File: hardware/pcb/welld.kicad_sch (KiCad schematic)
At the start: 0 parts

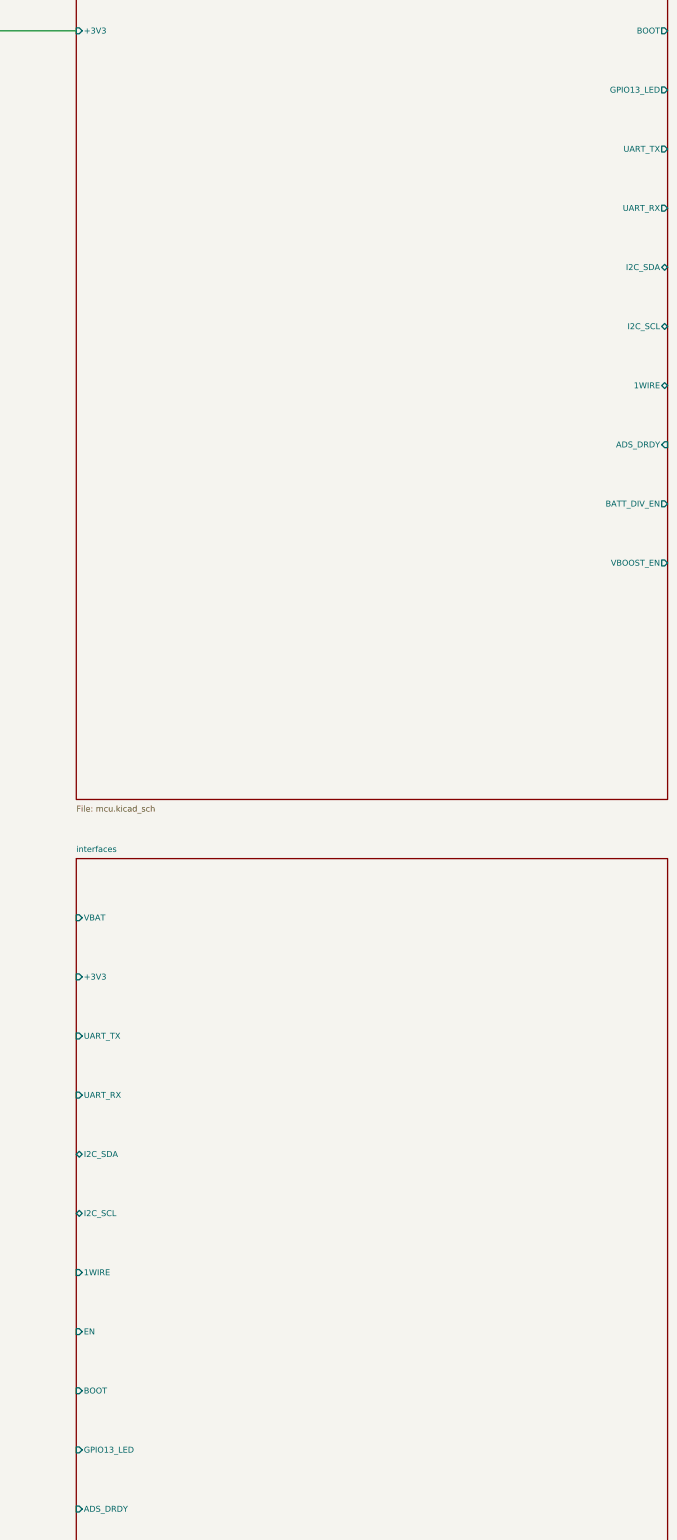
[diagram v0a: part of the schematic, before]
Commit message: hw(pcb): electrical review pass — fix 3V3 regulator variant, boost topology, GPIO13 LED conflict
Full electrical-correctness-gate review of the fresh-start design. Two of
the four CRITICALs from the 2026-05-25 senior review were resolved
incorrectly; this pass corrects them and fixes new findings:

- U1: AP63205WU is the 5 V fixed variant and the R_FBH/R_FBL values
  (560k/124k) assume a 0.6 V reference no AP6320x has — every
  combination overdrives the 3V3 rail. Swap to AP63203WU (3.3 V fixed),
  FB tied to +3V3, R_FBH/R_FBL marked DNP.
- MT3608B VLOOP: documented wiring was a buck topology and the BOM had
  no output rectifier (async boost cannot work without one). Corrected
  to VBAT→L1→SW, added D15 (SS34) and a Q3/Q4 load-disconnect so VBAT
  doesn't leak to the loop terminals through L1+D15 during deep sleep.
- Status LED moved GPIO13 → GPIO14: a green LED + 1k on GPIO13 holds
  the factory-reset strap LOW at boot → NVS wipe every boot. TP13 pad
  added for field factory reset.
- Battery divider reworked to high-side P-FET (Q5): the low-side switch
  left AIN2 biased above ADS1115 VDD through R7 (~14 uA sleep leak).
  C8 100nF → 1nF to fit the firmware's 1 ms enable window.
- TVS D8/D14 SMAJ28CA → SMAJ24CA (zero margin to CN3722 28 V abs max);
  C17 → 35 V/1206; C21 → 50 V; D6 footprint SOD-123 → SMB.
- /CHRG_SOLAR pull-up (R25), VBOOST_EN pull-down (R27), ESP32 EN RC
  (R15/C36) added; C25 duplicate bootstrap cap deleted; C16 assigned as
  U1 VIN bulk.
- schematic_connections.md rewritten pin-name-based with a symbol
  pin-number verification table and datasheet-verification blocker list;
  BOM/placement/guide/placement-script reconciled (phantom refdes,
  wrong ADS1115 pin numbers, mis-documented MPPT divider, shunt return
  path contradiction).

Flagged, not fixed: TP5100 cannot charge 2S from 5 V USB (step-down
charger) — needs an IC swap; schematic still has zero drawn wires; five
IC symbol pinouts pending datasheet verification before ordering.

Co-Auth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
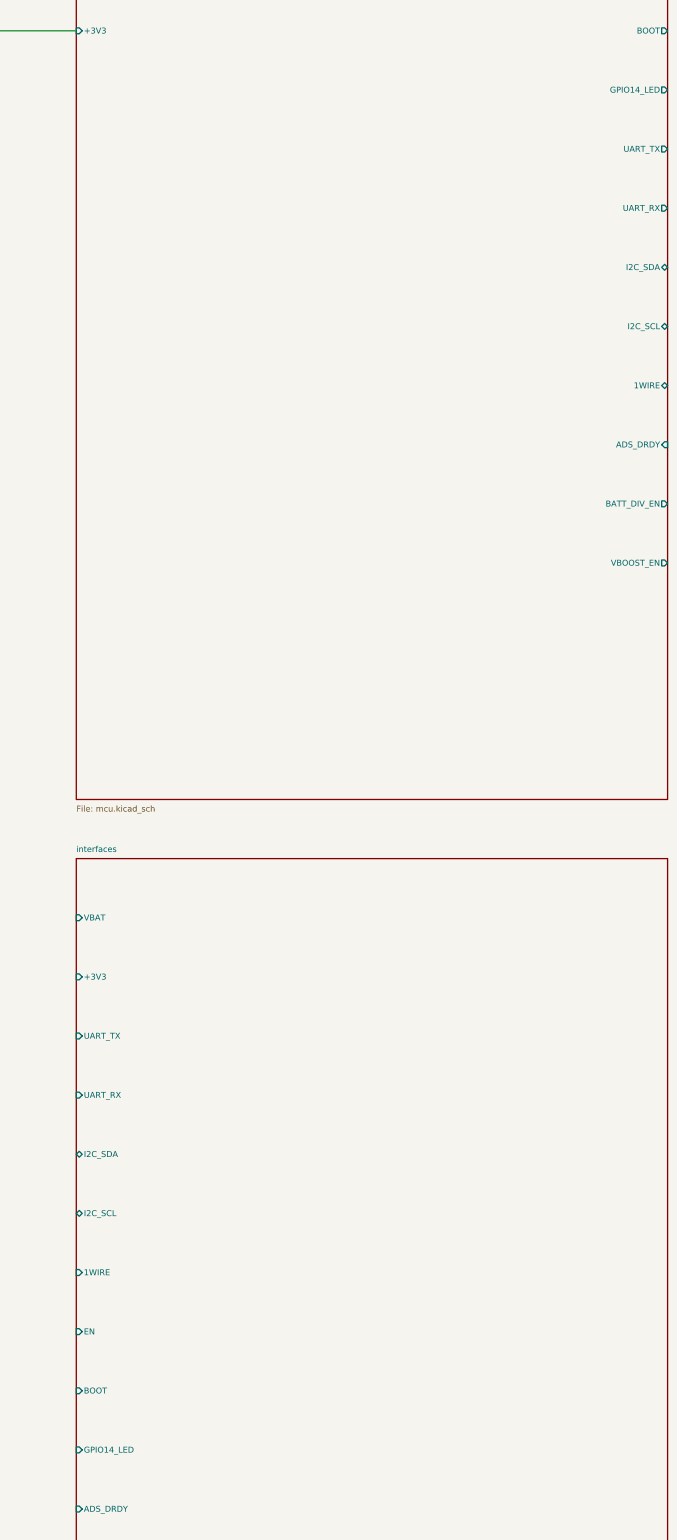
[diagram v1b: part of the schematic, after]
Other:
- sheet interfaces ports: added GPIO14_LED; removed GPIO13_LED
- sheet mcu ports: added GPIO14_LED; removed GPIO13_LED
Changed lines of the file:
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@@
 			)
 		)
-		(pin "GPIO13_LED" output
+		(pin "GPIO14_LED" output
 			(at 304.8 50.8 0)
 			(effects
@@
 			)
 		)
-		(pin "GPIO13_LED" input
+		(pin "GPIO14_LED" input
 			(at 177.8 342.9 180)
 			(effects

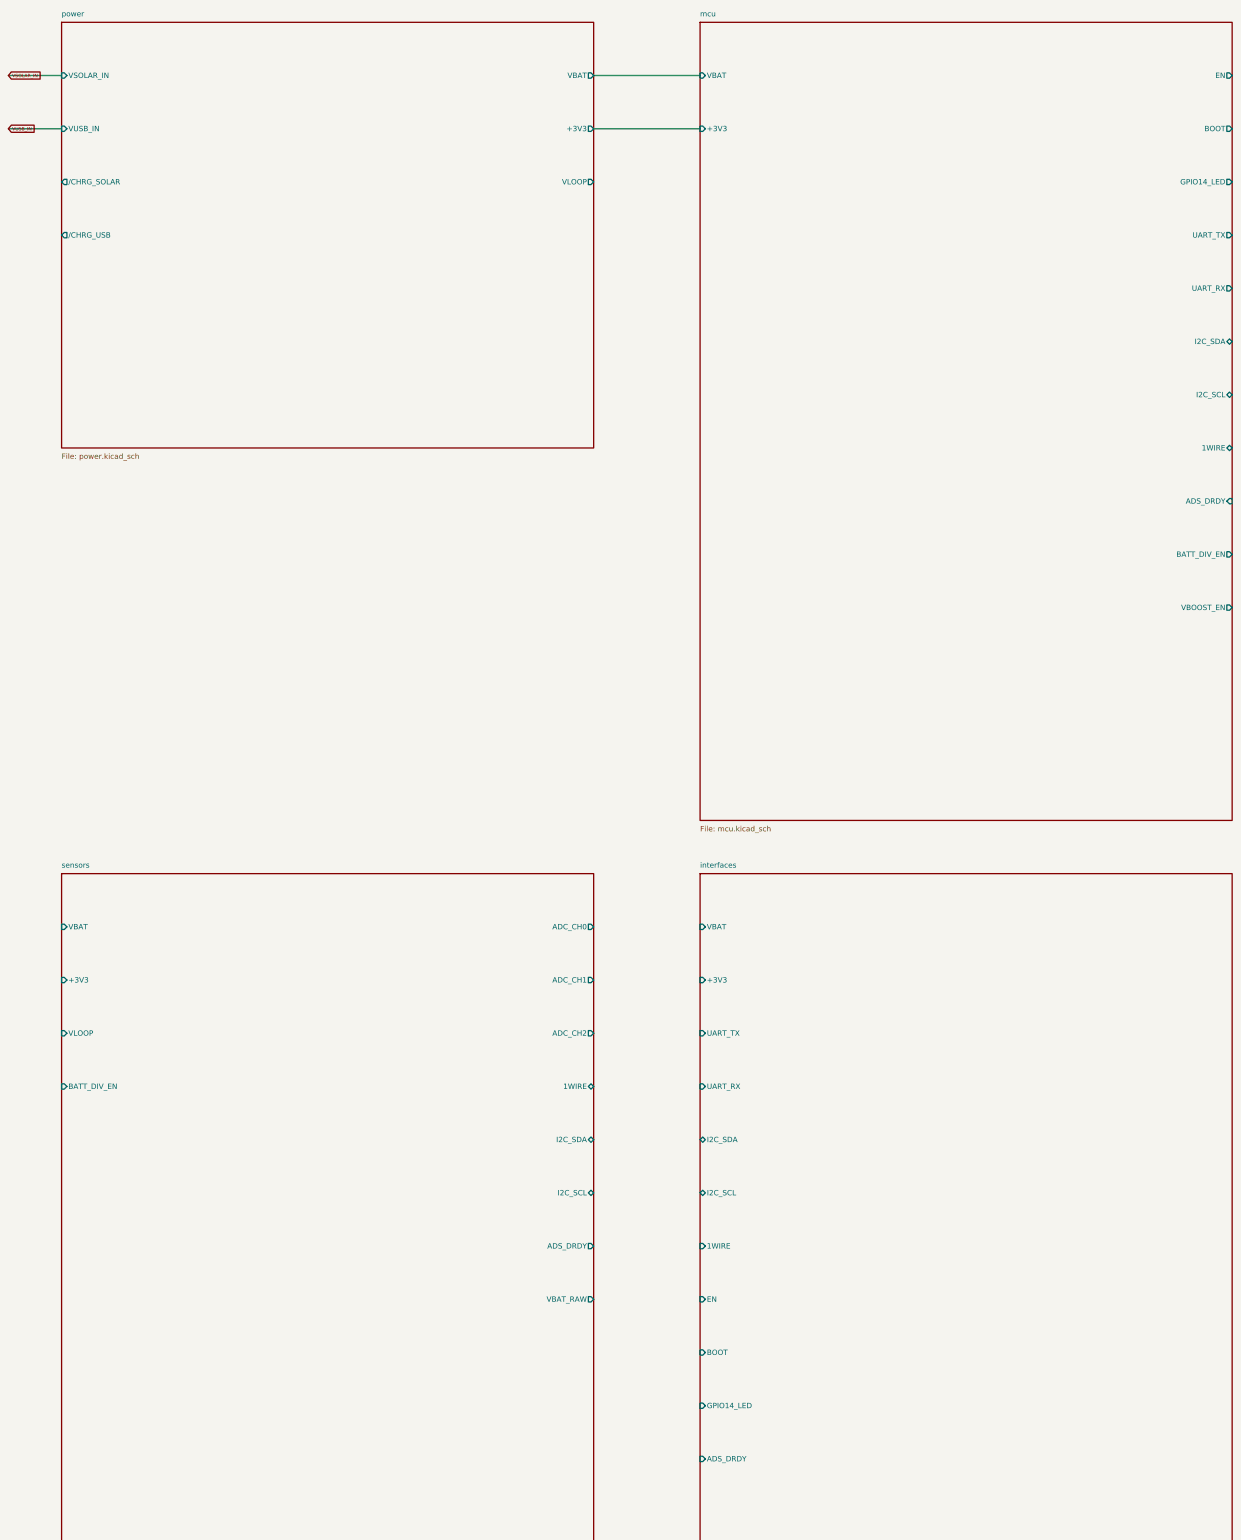
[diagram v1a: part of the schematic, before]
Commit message: hw(pcb): wiring pass — schematic fully wired, netlist machine-verified (0 mismatches)
All four sheets wired with stub+label connectivity (434 wires, 21
explicit no-connects, PWR_FLAGs on undriven rails): power rails on
global labels, cross-sheet signals on hierarchical labels + rebuilt
top-sheet pins (24 hierarchical nets; vestigial ADC_CH* pins deleted,
GPIO14_LED corrected to the mcu-local net it really is), sheet-local
nets on local labels.

Verification (kicad-cli for the KiCad-10 format is not installable
here): hardware/pcb/kicad_wire_script.py generates the connectivity
from an embedded intent table derived from schematic_connections.md;
hardware/pcb/netlist_check.py independently re-extracts pin->net
geometrically (union-find over wires/labels/sheet pins) and diffs —
395 pins, 77 nets, 0 mismatches (output committed). Native KiCad 10
ERC + resave queued for the first interactive open.

Notable resolutions (recorded as design change #17): AP63203 FB tied
to +3V3 with the DNP divider floated at its midpoint; MT3608B pin 6
etype relaxed to passive so C_BST wiring is ERC-legal; IP2326 DM/DP
floated with no-connects (adapter detection is a two-wire future
change); D11 oriented cathode-to-VLOOP; decorative corner power
symbols replaced with real rail connectivity.

placement_constraints.md: Group G rewritten for the IP2326 hot loop,
new Group L for the CN3722 external buck (Kelvin CSP/BAT pair).
Top remaining risk flagged in blockers: AP63203 BST is NC per the
wiring doc but the AP6320x family likely requires a BST-SW cap —
resolve before layout freeze.

Co-Authored-By: Claude Fable 5 <noreply@anthropic.com>
Claude-Session: https://claude.ai/code/session_01VtMFY5Q94iYbsNPpLcPJyK
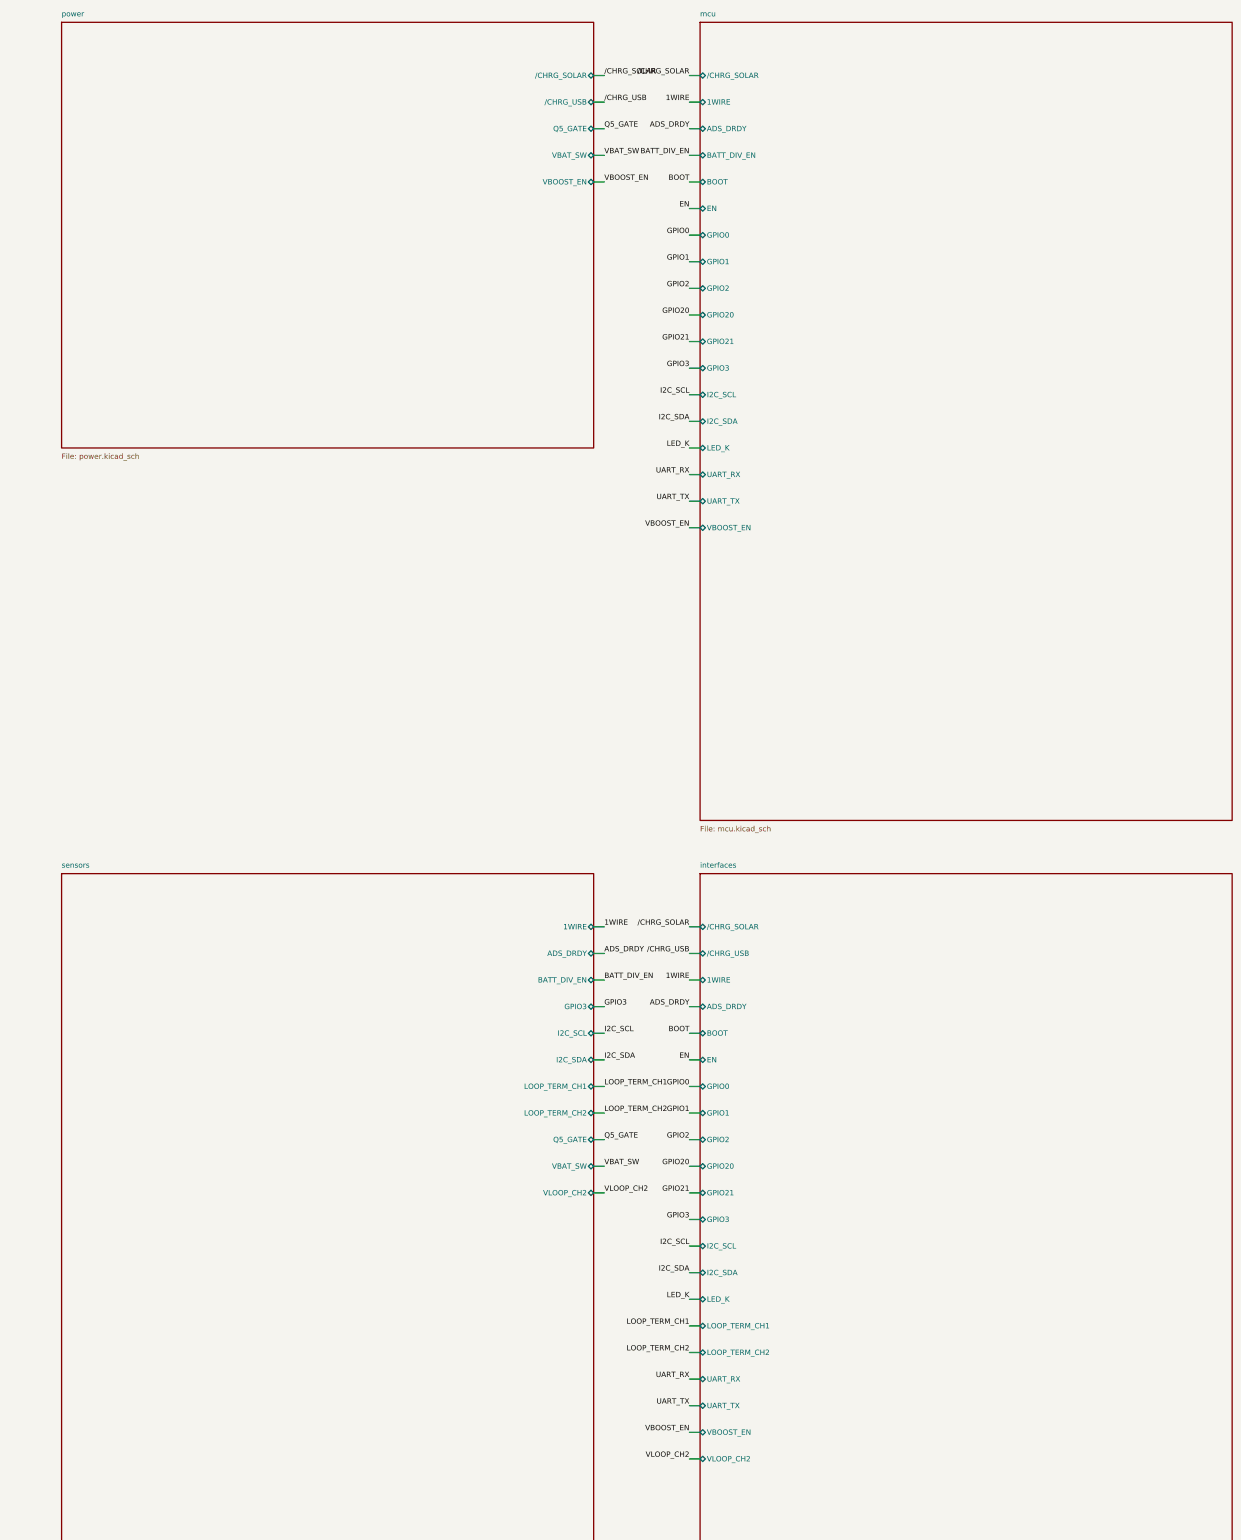
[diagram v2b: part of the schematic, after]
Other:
- sheet interfaces ports: added /CHRG_SOLAR, /CHRG_USB, GPIO0, GPIO1, GPIO2, GPIO20, GPIO21, GPIO3, LED_K, LOOP_TERM_CH1, LOOP_TERM_CH2, VBOOST_EN, VLOOP_CH2; removed +3V3, GPIO14_LED, VBAT
- sheet mcu ports: added /CHRG_SOLAR, GPIO0, GPIO1, GPIO2, GPIO20, GPIO21, GPIO3, LED_K; removed +3V3, GPIO14_LED, VBAT
- sheet power ports: added Q5_GATE, VBAT_SW, VBOOST_EN; removed +3V3, VBAT, VLOOP, VSOLAR_IN, VUSB_IN
- sheet sensors ports: added GPIO3, LOOP_TERM_CH1, LOOP_TERM_CH2, Q5_GATE, VBAT_SW, VLOOP_CH2; removed +3V3, ADC_CH0, ADC_CH1, ADC_CH2, VBAT, VBAT_RAW, VLOOP
